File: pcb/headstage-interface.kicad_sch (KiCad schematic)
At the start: 3 parts, among them J1 MOLC-110-01-S-Q_1, J2 MOLC-110-01-S-Q_1, J3 Conn_02x02_Odd_Even

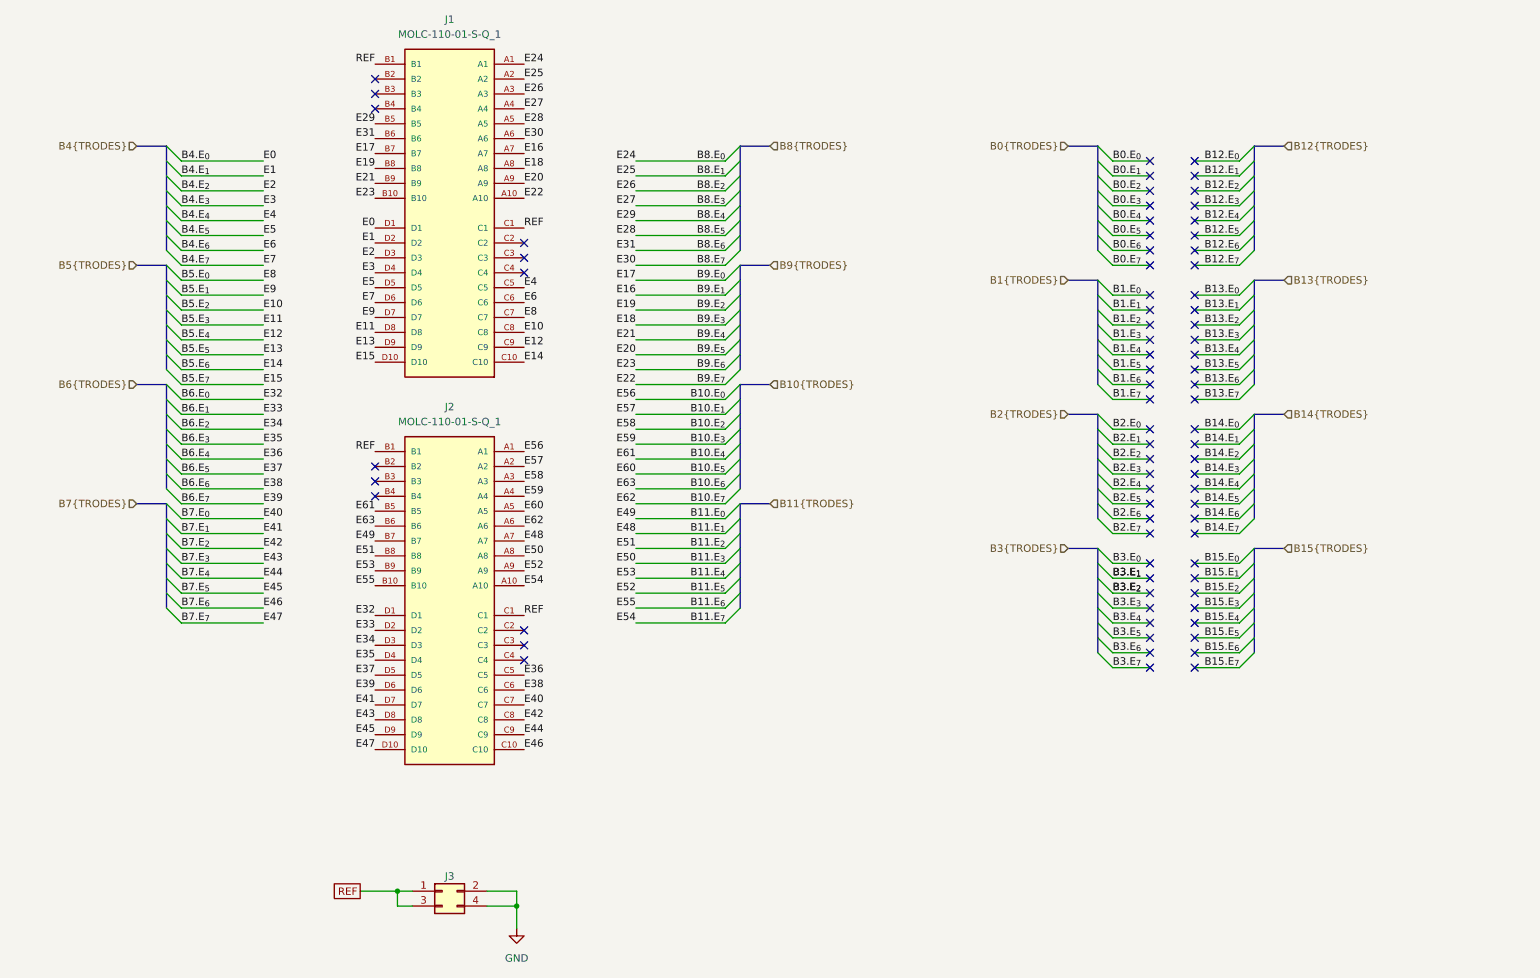
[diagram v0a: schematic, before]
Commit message: Revision B
- Added 220k resistor arrays in series with amplifier connections to
  simulate electrodes
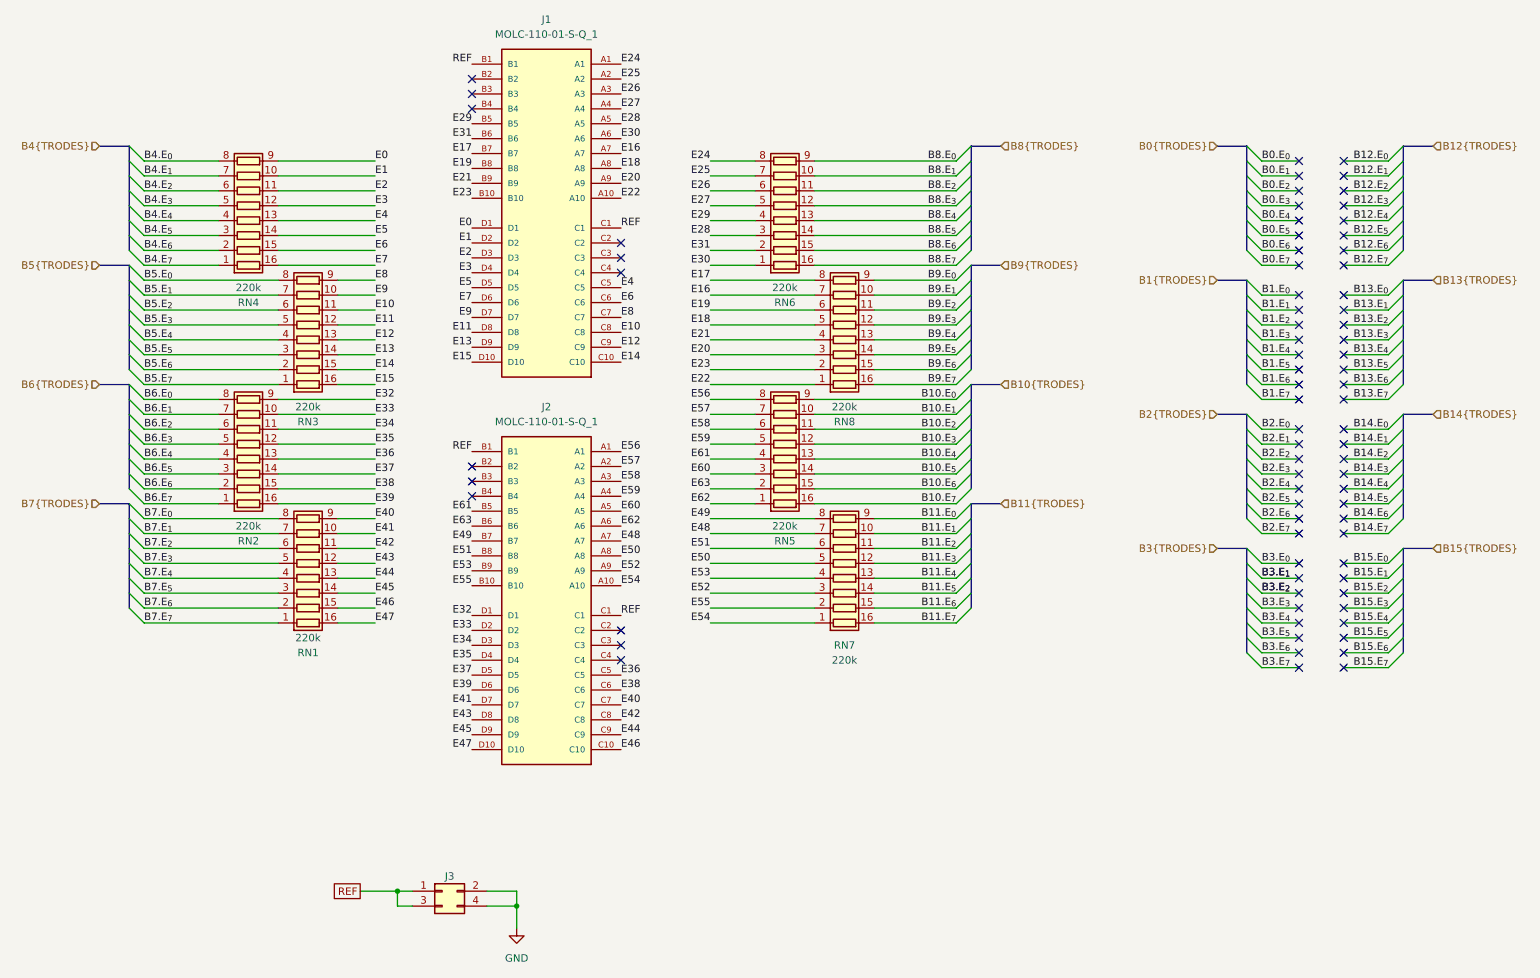
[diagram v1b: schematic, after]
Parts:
- added RN1, RN2, RN3, RN4, RN5, RN6, RN7, RN8: 220k, Resistor_SMD:R_Array_Convex_8x0602, symbol Device:R_Pack08
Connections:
- net B10.E_{0}: now also RN5.9 (R8.2); no longer J2.A1
- net B10.E_{1}: now also RN5.10 (R7.2); no longer J2.A2
- net B10.E_{2}: now also RN5.11 (R6.2); no longer J2.A3
- net B10.E_{3}: now also RN5.12 (R5.2); no longer J2.A4
- net B10.E_{4}: now also RN5.13 (R4.2); no longer J2.B5
- net B10.E_{5}: now also RN5.14 (R3.2); no longer J2.A5
- net B10.E_{6}: now also RN5.15 (R2.2); no longer J2.B6
- net B10.E_{7}: now also RN5.16 (R1.2); no longer J2.A6
- net B11.E_{0}: now also RN7.9 (R8.2); no longer J2.B7
- net B11.E_{1}: now also RN7.10 (R7.2); no longer J2.A7
- net B11.E_{2}: now also RN7.11 (R6.2); no longer J2.B8
- net B11.E_{3}: now also RN7.12 (R5.2); no longer J2.A8
- net B11.E_{4}: now also RN7.13 (R4.2); no longer J2.B9
- net B11.E_{5}: now also RN7.14 (R3.2); no longer J2.A9
- net B11.E_{6}: now also RN7.15 (R2.2); no longer J2.B10
- net B11.E_{7}: now also RN7.16 (R1.2); no longer J2.A10
- net B4.E_{0}: now also RN4.8 (R8.1); no longer J1.D1
- net B4.E_{1}: now also RN4.7 (R7.1); no longer J1.D2
- net B4.E_{2}: now also RN4.6 (R6.1); no longer J1.D3
- net B4.E_{3}: now also RN4.5 (R5.1); no longer J1.D4
- net B4.E_{4}: now also RN4.4 (R4.1); no longer J1.C5
- net B4.E_{5}: now also RN4.3 (R3.1); no longer J1.D5
- net B4.E_{6}: now also RN4.2 (R2.1); no longer J1.C6
- net B4.E_{7}: now also RN4.1 (R1.1); no longer J1.D6
- net B5.E_{0}: now also RN3.8 (R8.1); no longer J1.C7
- net B5.E_{1}: now also RN3.7 (R7.1); no longer J1.D7
- net B5.E_{2}: now also RN3.6 (R6.1); no longer J1.C8
- net B5.E_{3}: now also RN3.5 (R5.1); no longer J1.D8
- net B5.E_{4}: now also RN3.4 (R4.1); no longer J1.C9
- net B5.E_{5}: now also RN3.3 (R3.1); no longer J1.D9
- net B5.E_{6}: now also RN3.2 (R2.1); no longer J1.C10
- net B5.E_{7}: now also RN3.1 (R1.1); no longer J1.D10
- net B6.E_{0}: now also RN2.8 (R8.1); no longer J2.D1
- net B6.E_{1}: now also RN2.7 (R7.1); no longer J2.D2
- net B6.E_{2}: now also RN2.6 (R6.1); no longer J2.D3
- net B6.E_{3}: now also RN2.5 (R5.1); no longer J2.D4
- net B6.E_{4}: now also RN2.4 (R4.1); no longer J2.C5
- net B6.E_{5}: now also RN2.3 (R3.1); no longer J2.D5
- net B6.E_{6}: now also RN2.2 (R2.1); no longer J2.C6
- net B6.E_{7}: now also RN2.1 (R1.1); no longer J2.D6
- net B7.E_{0}: now also RN1.8 (R8.1); no longer J2.C7
- net B7.E_{1}: now also RN1.7 (R7.1); no longer J2.D7
- net B7.E_{2}: now also RN1.6 (R6.1); no longer J2.C8
- net B7.E_{3}: now also RN1.5 (R5.1); no longer J2.D8
- net B7.E_{4}: now also RN1.4 (R4.1); no longer J2.C9
- net B7.E_{5}: now also RN1.3 (R3.1); no longer J2.D9
- net B7.E_{6}: now also RN1.2 (R2.1); no longer J2.C10
- net B7.E_{7}: now also RN1.1 (R1.1); no longer J2.D10
- net B8.E_{0}: now also RN6.9 (R8.2); no longer J1.A1
- net B8.E_{1}: now also RN6.10 (R7.2); no longer J1.A2
- net B8.E_{2}: now also RN6.11 (R6.2); no longer J1.A3
- net B8.E_{3}: now also RN6.12 (R5.2); no longer J1.A4
- net B8.E_{4}: now also RN6.13 (R4.2); no longer J1.B5
- net B8.E_{5}: now also RN6.14 (R3.2); no longer J1.A5
- net B8.E_{6}: now also RN6.15 (R2.2); no longer J1.B6
- net B8.E_{7}: now also RN6.16 (R1.2); no longer J1.A6
- net B9.E_{0}: now also RN8.9 (R8.2); no longer J1.B7
- net B9.E_{1}: now also RN8.10 (R7.2); no longer J1.A7
- net B9.E_{2}: now also RN8.11 (R6.2); no longer J1.B8
- net B9.E_{3}: now also RN8.12 (R5.2); no longer J1.A8
- net B9.E_{4}: now also RN8.13 (R4.2); no longer J1.B9
- net B9.E_{5}: now also RN8.14 (R3.2); no longer J1.A9
- net B9.E_{6}: now also RN8.15 (R2.2); no longer J1.B10
- net B9.E_{7}: now also RN8.16 (R1.2); no longer J1.A10
- new net E0: J1.D1, RN4.9 (R8.2)
- new net E1: J1.D2, RN4.10 (R7.2)
- new net E10: J1.C8, RN3.11 (R6.2)
- new net E11: J1.D8, RN3.12 (R5.2)
- new net E12: J1.C9, RN3.13 (R4.2)
- new net E13: J1.D9, RN3.14 (R3.2)
- new net E14: J1.C10, RN3.15 (R2.2)
- new net E15: J1.D10, RN3.16 (R1.2)
- new net E16: J1.A7, RN8.7 (R7.1)
- new net E17: J1.B7, RN8.8 (R8.1)
- new net E18: J1.A8, RN8.5 (R5.1)
- new net E19: J1.B8, RN8.6 (R6.1)
- new net E2: J1.D3, RN4.11 (R6.2)
- new net E20: J1.A9, RN8.3 (R3.1)
- new net E21: J1.B9, RN8.4 (R4.1)
- new net E22: J1.A10, RN8.1 (R1.1)
- new net E23: J1.B10, RN8.2 (R2.1)
- new net E24: J1.A1, RN6.8 (R8.1)
- new net E25: J1.A2, RN6.7 (R7.1)
- new net E26: J1.A3, RN6.6 (R6.1)
- new net E27: J1.A4, RN6.5 (R5.1)
- new net E28: J1.A5, RN6.3 (R3.1)
- new net E29: J1.B5, RN6.4 (R4.1)
- new net E3: J1.D4, RN4.12 (R5.2)
- new net E30: J1.A6, RN6.1 (R1.1)
- new net E31: J1.B6, RN6.2 (R2.1)
- new net E32: J2.D1, RN2.9 (R8.2)
- new net E33: J2.D2, RN2.10 (R7.2)
- new net E34: J2.D3, RN2.11 (R6.2)
- new net E35: J2.D4, RN2.12 (R5.2)
- new net E36: J2.C5, RN2.13 (R4.2)
- new net E37: J2.D5, RN2.14 (R3.2)
- new net E38: J2.C6, RN2.15 (R2.2)
- new net E39: J2.D6, RN2.16 (R1.2)
- new net E4: J1.C5, RN4.13 (R4.2)
- new net E40: J2.C7, RN1.9 (R8.2)
- new net E41: J2.D7, RN1.10 (R7.2)
- new net E42: J2.C8, RN1.11 (R6.2)
- new net E43: J2.D8, RN1.12 (R5.2)
- new net E44: J2.C9, RN1.13 (R4.2)
- new net E45: J2.D9, RN1.14 (R3.2)
- new net E46: J2.C10, RN1.15 (R2.2)
- new net E47: J2.D10, RN1.16 (R1.2)
- new net E48: J2.A7, RN7.7 (R7.1)
- new net E49: J2.B7, RN7.8 (R8.1)
- new net E5: J1.D5, RN4.14 (R3.2)
- new net E50: J2.A8, RN7.5 (R5.1)
- new net E51: J2.B8, RN7.6 (R6.1)
- new net E52: J2.A9, RN7.3 (R3.1)
- new net E53: J2.B9, RN7.4 (R4.1)
- new net E54: J2.A10, RN7.1 (R1.1)
- new net E55: J2.B10, RN7.2 (R2.1)
- new net E56: J2.A1, RN5.8 (R8.1)
- new net E57: J2.A2, RN5.7 (R7.1)
- new net E58: J2.A3, RN5.6 (R6.1)
- new net E59: J2.A4, RN5.5 (R5.1)
- new net E6: J1.C6, RN4.15 (R2.2)
- new net E60: J2.A5, RN5.3 (R3.1)
- new net E61: J2.B5, RN5.4 (R4.1)
- new net E62: J2.A6, RN5.1 (R1.1)
- new net E63: J2.B6, RN5.2 (R2.1)
- new net E7: J1.D6, RN4.16 (R1.2)
- new net E8: J1.C7, RN3.9 (R8.2)
- new net E9: J1.D7, RN3.10 (R7.2)
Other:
- moved on the sheet: J1, J2

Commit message: Revision B
- Widened traces to 0.2 mm
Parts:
- J1, J2: MPN (none) -> MOLC-110-01-S-Q_1
- J3: value Conn_02x02_Odd_Even -> M20-8760242
- RN1, RN2, RN3, RN4, RN5, RN6, RN7, RN8: Tolerance (none) -> 5%
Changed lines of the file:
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@@
+			)
+		)
+		(property "Temp. Co." ""
+			(at 69.85 78.74 90)
+			(effects
+				(font
+					(size 1.27 1.27)
+				)
+				(hide yes)
+			)
+		)
+		(property "Tolerance" "5%"
+			(at 69.85 78.74 90)
+			(effects
+				(font
+					(size 1.27 1.27)
+				)
+				(hide yes)
 			)
 		)
@@
 			)
 		)
+		(property "Temp. Co." ""
+			(at 59.69 58.42 90)
+			(effects
+				(font
+					(size 1.27 1.27)
+				)
+				(hide yes)
+			)
+		)
+		(property "Tolerance" "5%"
+			(at 59.69 58.42 90)
+			(effects
+				(font
+					(size 1.27 1.27)
+				)
+				(hide yes)
+			)
+		)
 		(pin "12"
 		)
@@
 			)
 		)
+		(property "MPN" "MOLC-110-01-S-Q_1"
+			(at 110.49 125.73 0)
+			(effects
+				(font
+					(size 1.27 1.27)
+				)
+				(hide yes)
+			)
+		)
+		(property "Temp. Co." ""
+			(at 110.49 125.73 0)
+			(effects
+				(font
+					(size 1.27 1.27)
+				)
+				(hide yes)
+			)
+		)
 		(pin "B2"
 		)
@@
 			)
 		)
+		(property "Temp. Co." ""
+			(at 151.13 58.42 90)
+			(effects
+				(font
+					(size 1.27 1.27)
+				)
+				(hide yes)
+			)
+		)
+		(property "Tolerance" "5%"
+			(at 151.13 58.42 90)
+			(effects
+				(font
+					(size 1.27 1.27)
+				)
+				(hide yes)
+			)
+		)
 		(pin "12"
 		)
@@
 			)
 		)
+		(property "Temp. Co." ""
+			(at 161.29 119.38 90)
+			(effects
+				(font
+					(size 1.27 1.27)
+				)
+				(hide yes)
+			)
+		)
+		(property "Tolerance" "5%"
+			(at 161.29 119.38 90)
+			(effects
+				(font
+					(size 1.27 1.27)
+				)
+				(hide yes)
+			)
+		)
 		(pin "12"
 		)
@@
 		(dnp no)
 		(property "Reference" "J3"
-			(at 93.98 172.72 0)
-			(effects
-				(font
-					(size 1.27 1.27)
-				)
-			)
-		)
-		(property "Value" "Conn_02x02_Odd_Even"
+			(at 93.98 168.91 0)
+			(effects
+				(font
+					(size 1.27 1.27)
+				)
+			)
+		)
+		(property "Value" "M20-8760242"
 			(at 93.98 171.45 0)
 			(effects
@@
 					(size 1.27 1.27)
 				)
-				(hide yes)
 			)
 		)
@@
 		)
 		(property "OEPSPN" "OEPS070099"
+			(at 92.71 175.26 0)
+			(effects
+				(font
+					(size 1.27 1.27)
+				)
+				(hide yes)
+			)
+		)
+		(property "Temp. Co." ""
 			(at 92.71 175.26 0)
 			(effects
@@
 			)
 		)
+		(property "Temp. Co." ""
+			(at 161.29 78.74 90)
+			(effects
+				(font
+					(size 1.27 1.27)
+				)
+				(hide yes)
+			)
+		)
+		(property "Tolerance" "5%"
+			(at 161.29 78.74 90)
+			(effects
+				(font
+					(size 1.27 1.27)
+				)
+				(hide yes)
+			)
+		)
 		(pin "12"
 		)
@@
 			)
 		)
+		(property "MPN" "MOLC-110-01-S-Q_1"
+			(at 110.49 59.69 0)
+			(effects
+				(font
+					(size 1.27 1.27)
+				)
+				(hide yes)
+			)
+		)
+		(property "Temp. Co." ""
+			(at 110.49 59.69 0)
+			(effects
+				(font
+					(size 1.27 1.27)
+				)
+				(hide yes)
+			)
+		)
 		(pin "B2"
 		)
@@
 			)
 		)
+		(property "Temp. Co." ""
+			(at 69.85 119.38 90)
+			(effects
+				(font
+					(size 1.27 1.27)
+				)
+				(hide yes)
+			)
+		)
+		(property "Tolerance" "5%"
+			(at 69.85 119.38 90)
+			(effects
+				(font
+					(size 1.27 1.27)
+				)
+				(hide yes)
+			)
+		)
 		(pin "12"
 		)
@@
 			)
 		)
+		(property "Temp. Co." ""
+			(at 59.69 99.06 90)
+			(effects
+				(font
+					(size 1.27 1.27)
+				)
+				(hide yes)
+			)
+		)
+		(property "Tolerance" "5%"
+			(at 59.69 99.06 90)
+			(effects
+				(font
+					(size 1.27 1.27)
+				)
+				(hide yes)
+			)
+		)
 		(pin "12"
 		)
@@
 			(at 151.13 99.06 90)
 			(effects
+				(font
+					(size 1.27 1.27)
+				)
+				(hide yes)
+			)
+		)
+		(property "Temp. Co." ""
+			(at 151.13 99.06 90)
+			(effects
+				(font
+					(size 1.27 1.27)
+				)
+				(hide yes)
+			)
+		)
+		(property "Tolerance" "5%"
+			(at 151.13 99.06 90)
+			(effects
